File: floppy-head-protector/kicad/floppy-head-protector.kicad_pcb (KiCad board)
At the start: 2 copper layers, 133 x 157 mm, 0 parts

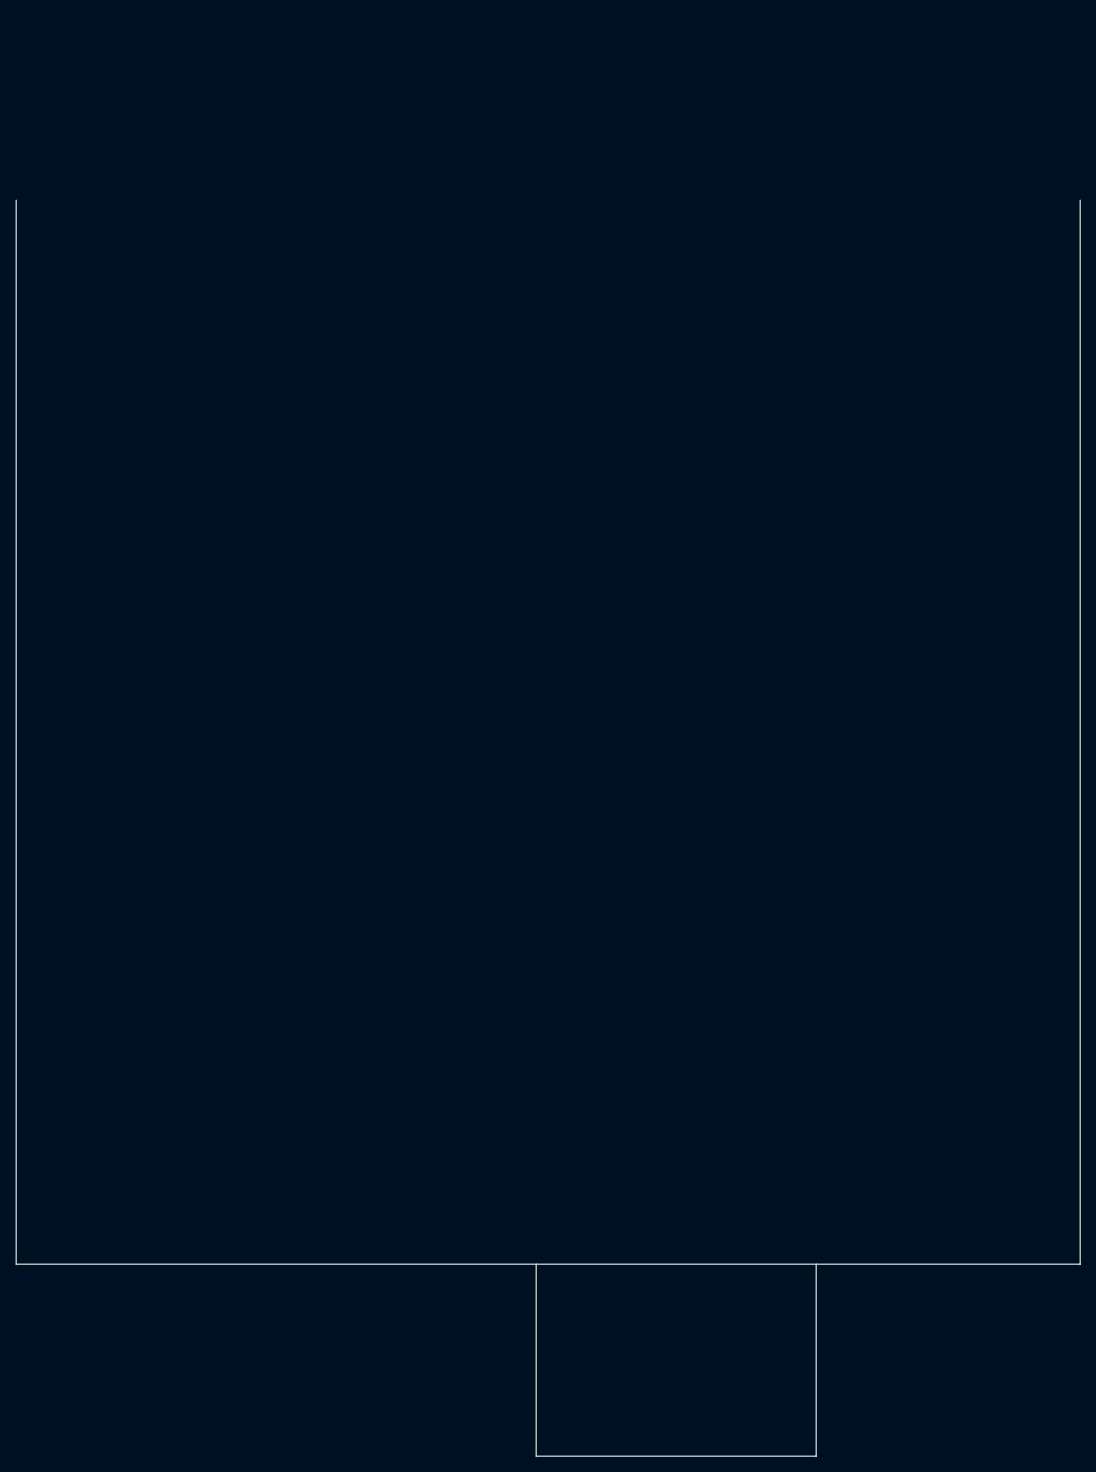
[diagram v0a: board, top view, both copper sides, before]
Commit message: WIP FHP: outline completed
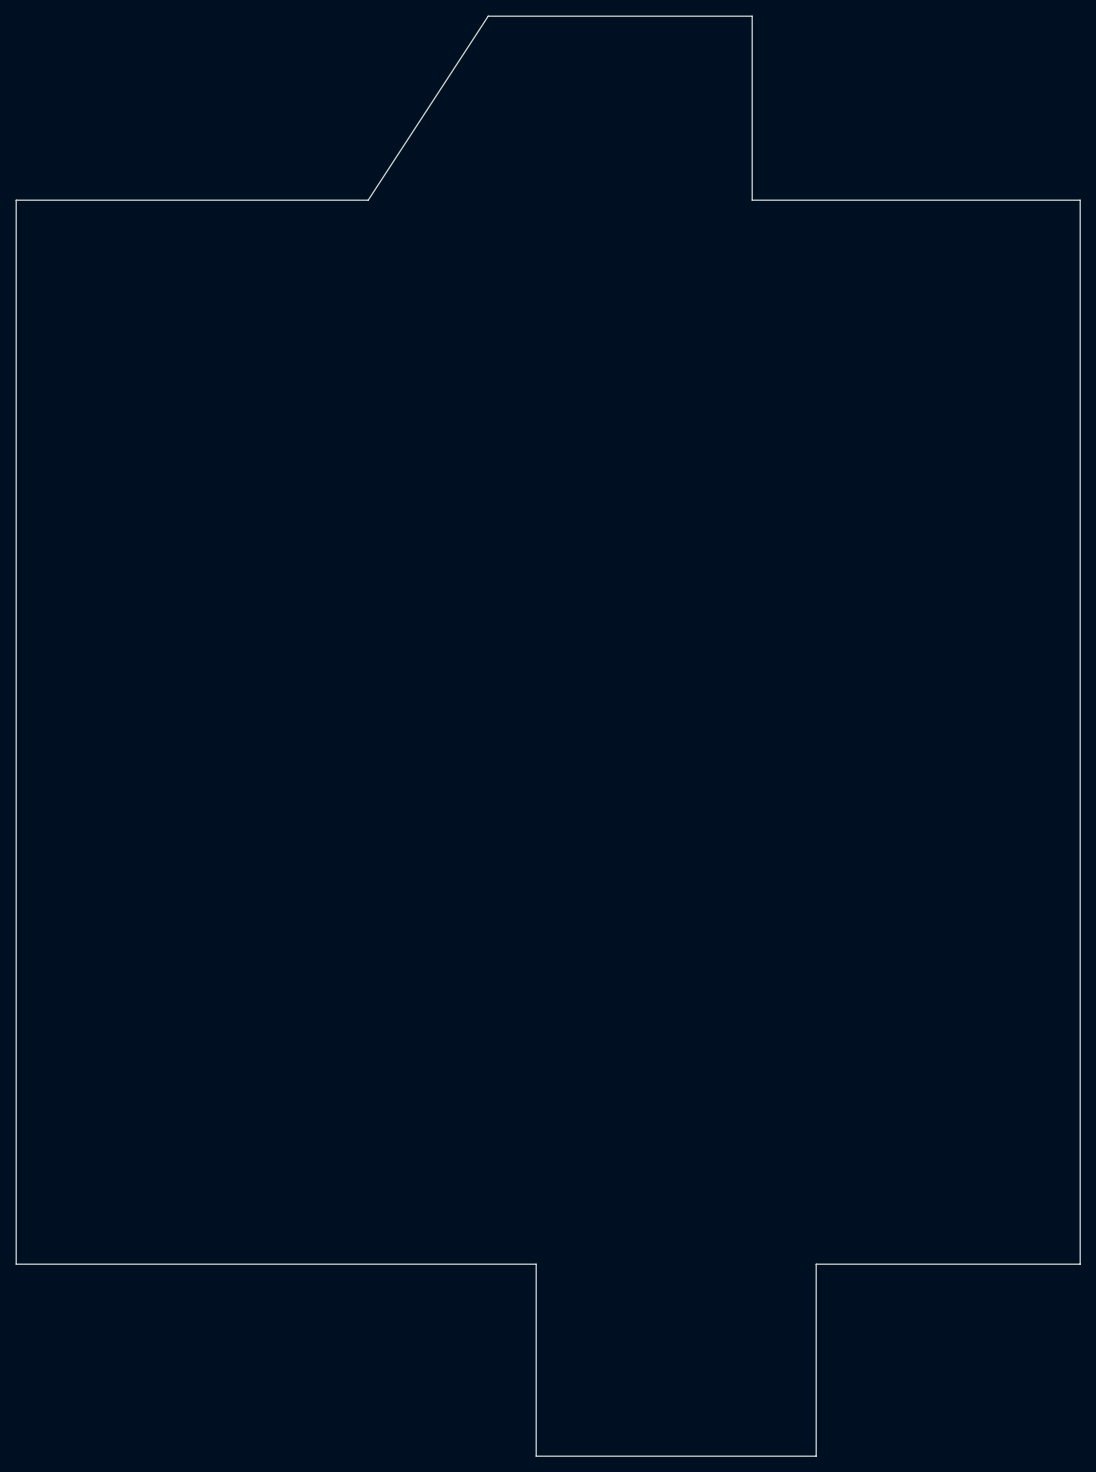
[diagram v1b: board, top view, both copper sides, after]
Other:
- board size 133 x 157 mm -> 133 x 180 mm
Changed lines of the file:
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@@
+	)
+	(gr_line
+		(start 163 30)
+		(end 122 30)
+		(stroke
+			(width 0.05)
+			(type solid)
+		)
+		(layer "Edge.Cuts")
 	)
 	(gr_line
 		(start 130 163)
 		(end 130 187)
+		(stroke
+			(width 0.05)
+			(type solid)
+		)
+		(layer "Edge.Cuts")
+	)
+	(gr_line
+		(start 74 30)
+		(end 89 7)
+		(stroke
+			(width 0.05)
+			(type solid)
+		)
+		(layer "Edge.Cuts")
+	)
+	(gr_line
+		(start 122 30)
+		(end 122 7)
 		(stroke
 			(width 0.05)
@@
 	)
 	(gr_line
+		(start 122 7)
+		(end 89 7)
+		(stroke
+			(width 0.05)
+			(type solid)
+		)
+		(layer "Edge.Cuts")
+	)
+	(gr_line
 		(start 30 163)
+		(end 95 163)
+		(stroke
+			(width 0.05)
+			(type solid)
+		)
+		(layer "Edge.Cuts")
+	)
+	(gr_line
+		(start 30 30)
+		(end 74 30)
+		(stroke
+			(width 0.05)
+			(type solid)
+		)
+		(layer "Edge.Cuts")
+	)
+	(gr_line
+		(start 130 163)
 		(end 163 163)
 		(stroke

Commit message: WIP FHP: Shorten by 3mm horizontal and vertical
- It was 1mm too large
- Remove 2 more mm because knife will cut a bit away from edge
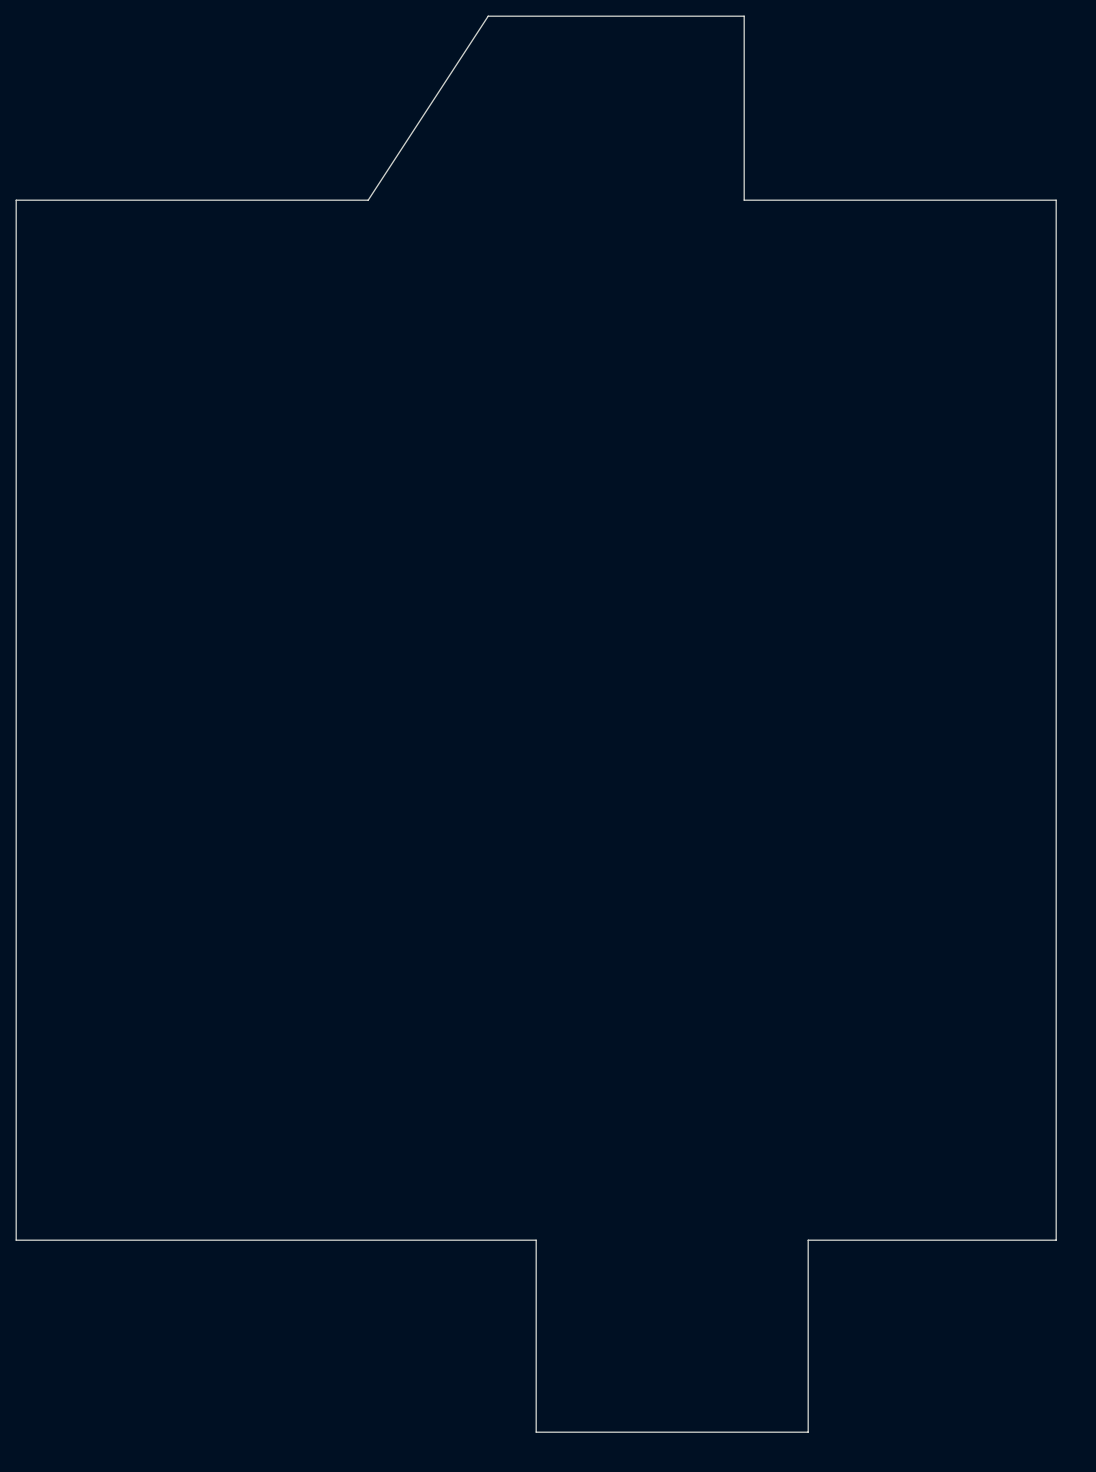
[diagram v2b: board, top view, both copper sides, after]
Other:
- board size 133 x 180 mm -> 130 x 177 mm
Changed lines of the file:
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@@
 	(net 0 "")
 	(gr_line
-		(start 95 187)
-		(end 130 187)
+		(start 95 184)
+		(end 129 184)
 		(stroke
 			(width 0.05)
@@
 	)
 	(gr_line
-		(start 95 163)
-		(end 95 187)
+		(start 95 160)
+		(end 95 184)
 		(stroke
 			(width 0.05)
@@
 	)
 	(gr_line
-		(start 163 30)
-		(end 122 30)
+		(start 121 30)
+		(end 160 30)
 		(stroke
 			(width 0.05)
@@
 	)
 	(gr_line
-		(start 130 163)
-		(end 130 187)
+		(start 129 160)
+		(end 129 184)
 		(stroke
 			(width 0.05)
@@
 	)
 	(gr_line
-		(start 122 30)
-		(end 122 7)
+		(start 121 30)
+		(end 121 7)
 		(stroke
 			(width 0.05)
@@
 	(gr_line
 		(start 30 30)
-		(end 30 163)
+		(end 30 160)
 		(stroke
 			(width 0.05)
@@
 	)
 	(gr_line
-		(start 122 7)
-		(end 89 7)
+		(start 89 7)
+		(end 121 7)
 		(stroke
 			(width 0.05)
@@
 	)
 	(gr_line
-		(start 30 163)
-		(end 95 163)
+		(start 30 160)
+		(end 95 160)
 		(stroke
 			(width 0.05)
@@
 	)
 	(gr_line
-		(start 130 163)
-		(end 163 163)
+		(start 129 160)
+		(end 160 160)
 		(stroke
 			(width 0.05)
-			(type default)
+			(type solid)
 		)
 		(layer "Edge.Cuts")
 	)
 	(gr_line
-		(start 163 30)
-		(end 163 163)
+		(start 160 30)
+		(end 160 160)
 		(stroke
 			(width 0.05)
